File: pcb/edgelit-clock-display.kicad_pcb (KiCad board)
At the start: 2 copper layers, 84 x 51 mm, 42 parts, among them J1 Conn_01x03, J2 Conn_01x03

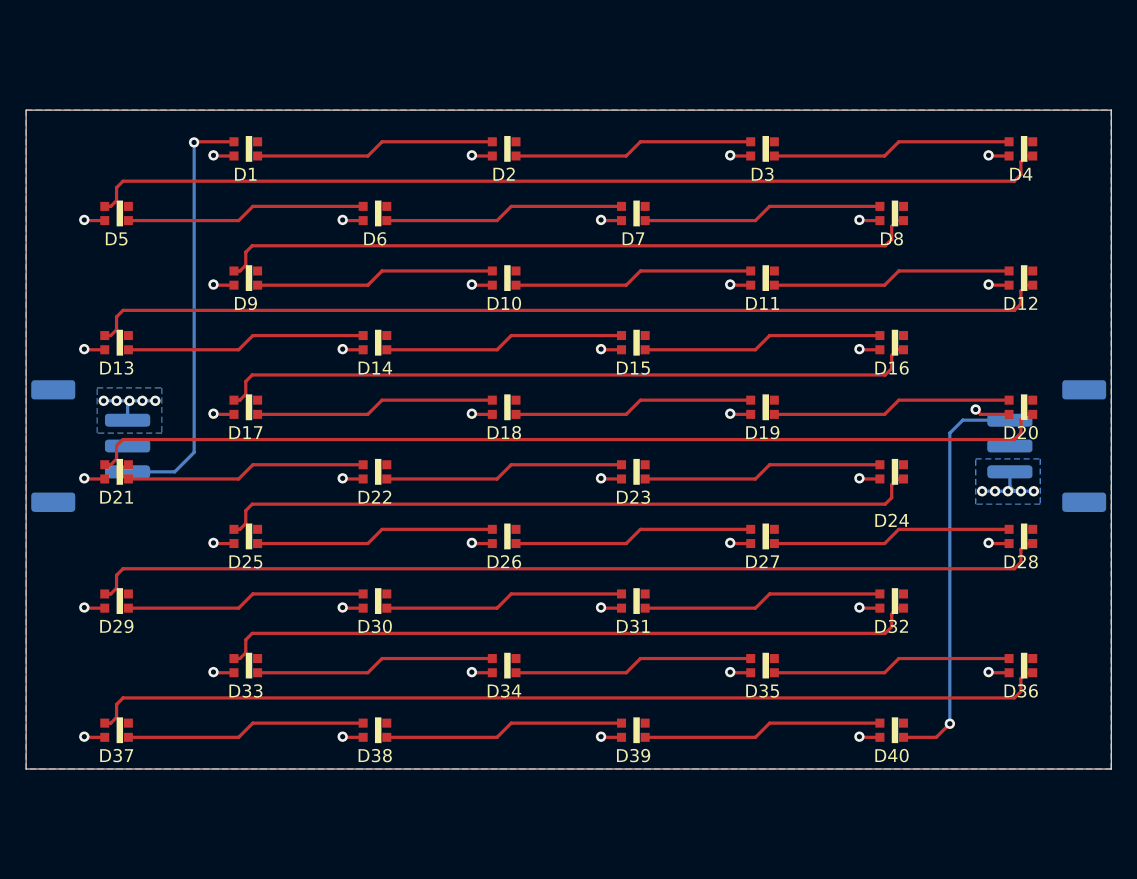
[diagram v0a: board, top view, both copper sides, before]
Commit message: Resized for a 30mm digit width, with 5mm between digits
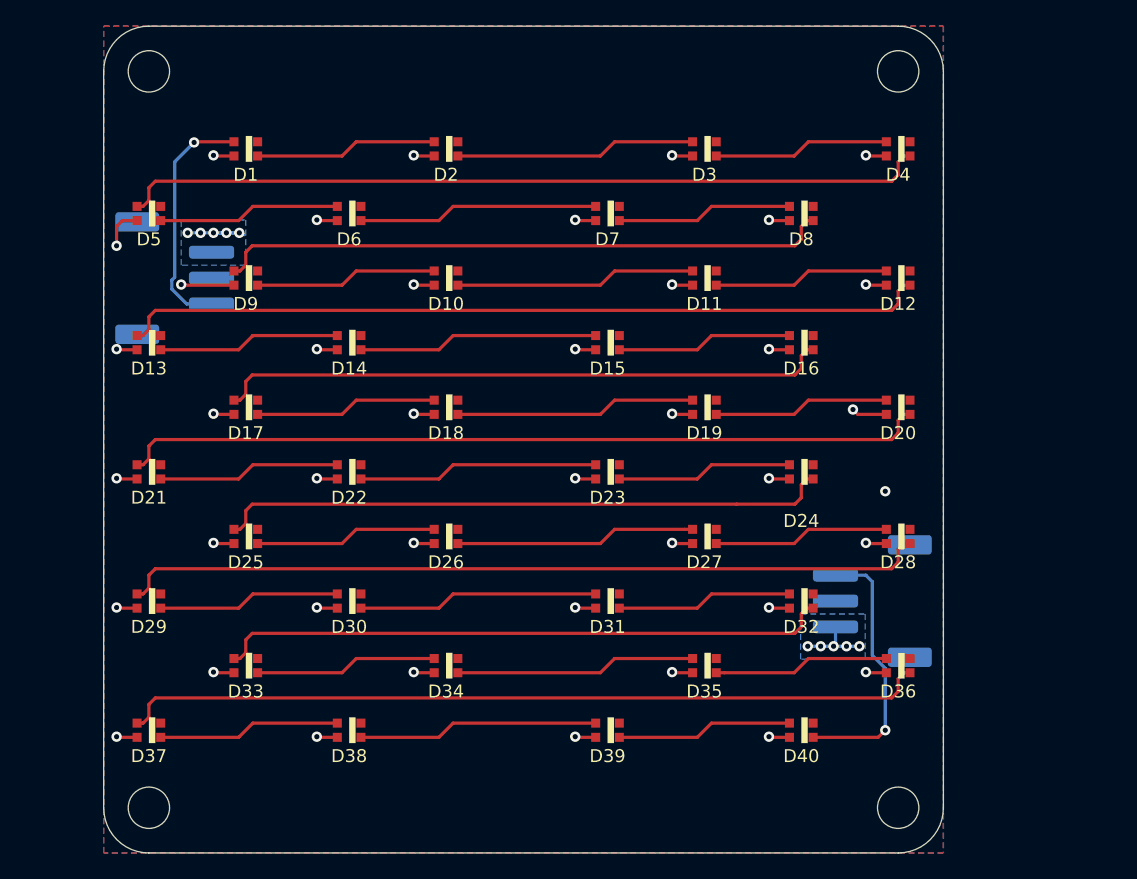
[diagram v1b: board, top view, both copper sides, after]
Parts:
- added H1: MountingHole, Mounting_Holes:MountingHole_3.2mm_M3_DIN965, F.Cu at (92.5, 74.0)
- added H2: MountingHole, Mounting_Holes:MountingHole_3.2mm_M3_DIN965, F.Cu at (150.5, 74.0)
- added H3: MountingHole, Mounting_Holes:MountingHole_3.2mm_M3_DIN965, F.Cu at (92.5, 131.0)
- added H4: MountingHole, Mounting_Holes:MountingHole_3.2mm_M3_DIN965, F.Cu at (150.5, 131.0)
- moved J2 18.1 mm to (148.5, 115.0)
- moved J1 14.5 mm to (94.5, 90.0)
- moved D12 9.50 mm to (150.5, 90.0)
- moved D20 9.50 mm to (150.5, 100.0)
- moved D28 9.50 mm to (150.5, 110.0)
- moved D36 9.50 mm to (150.5, 120.0)
- moved D4 9.50 mm to (150.5, 80.0)
- moved D16 7.00 mm to (143.0, 95.0)
- moved D24 7.00 mm to (143.0, 105.0)
- moved D32 7.00 mm to (143.0, 115.0)
- moved D40 7.00 mm to (143.0, 125.0)
- moved D8 7.00 mm to (143.0, 85.0)
- moved D10 4.50 mm to (115.5, 90.0)
- moved D11 4.50 mm to (135.5, 90.0)
- moved D18 4.50 mm to (115.5, 100.0)
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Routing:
- net Net-(D1-Pad4): track 32.9 -> 18.7 mm
- net Net-(D4-Pad2): track 74.6 -> 62.6 mm
- net Net-(D12-Pad2): track 74.6 -> 62.6 mm
- net Net-(D36-Pad2): track 74.6 -> 62.6 mm
- net Net-(D28-Pad2): track 74.6 -> 62.6 mm
- net Net-(D20-Pad2): track 74.6 -> 62.6 mm
- net Net-(D40-Pad2): track 31.6 -> 20.8 mm
- net Net-(D8-Pad2): track 54.6 -> 47.6 mm
- net Net-(D32-Pad2): track 54.6 -> 47.6 mm
- net Net-(D24-Pad2): track 54.6 -> 47.6 mm
- net Net-(D16-Pad2): track 54.6 -> 47.6 mm
- net Net-(D7-Pad2): track 18.6 -> 13.6 mm
- net Net-(D39-Pad2): track 18.6 -> 13.6 mm
- net Net-(D35-Pad2): track 18.6 -> 13.6 mm
- net Net-(D31-Pad2): track 18.6 -> 13.6 mm
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- removed copper zone on B.Cu, net (none)
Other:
- board size 84 x 51 mm -> 65 x 64 mm
